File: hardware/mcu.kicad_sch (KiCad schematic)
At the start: 4 parts, among them U3 STM32G0C1KCTxN

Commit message: Fixes after review
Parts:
- added C1, C24: 100n, Capacitor_SMD:C_0603_1608Metric_Pad1.08x0.95mm_HandSolder, symbol Device:C_Small
- R10, R11, R9: value 1k -> 33R
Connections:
- net +3.3V: now also C1.1, C24.1
- net GND: now also C1.2, C24.2
- net VN_RX: now also U3.31 (PB7); no longer U3.30 (PB6)
- net VN_TX: now also U3.30 (PB6); no longer U3.31 (PB7)
- net VN_SNC_IN renamed VN_GNSS_SYNC
- net VN_SNC_OUT: no longer names the net of U3.2 (PC14)
- no-connect marks 7 -> 8

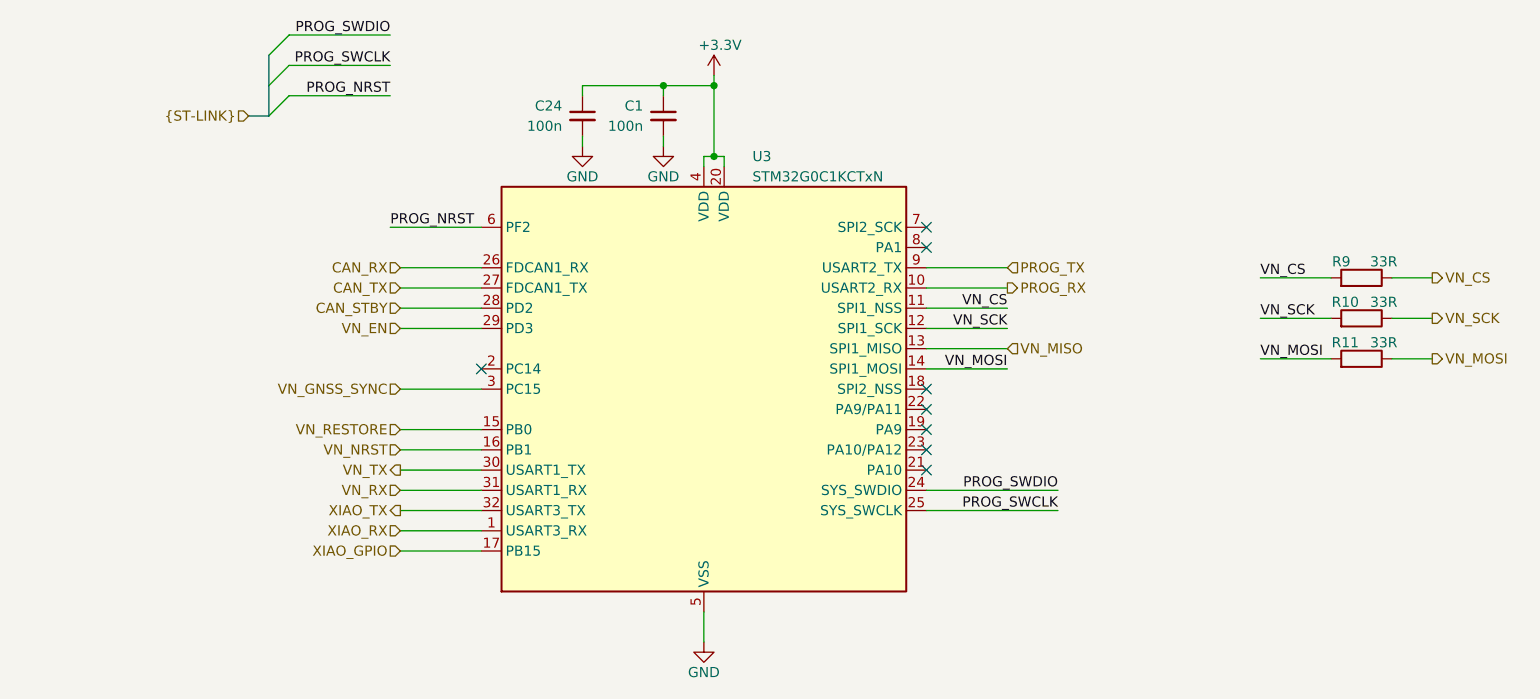
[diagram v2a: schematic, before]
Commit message: Fixes after review and mouser links for most components added
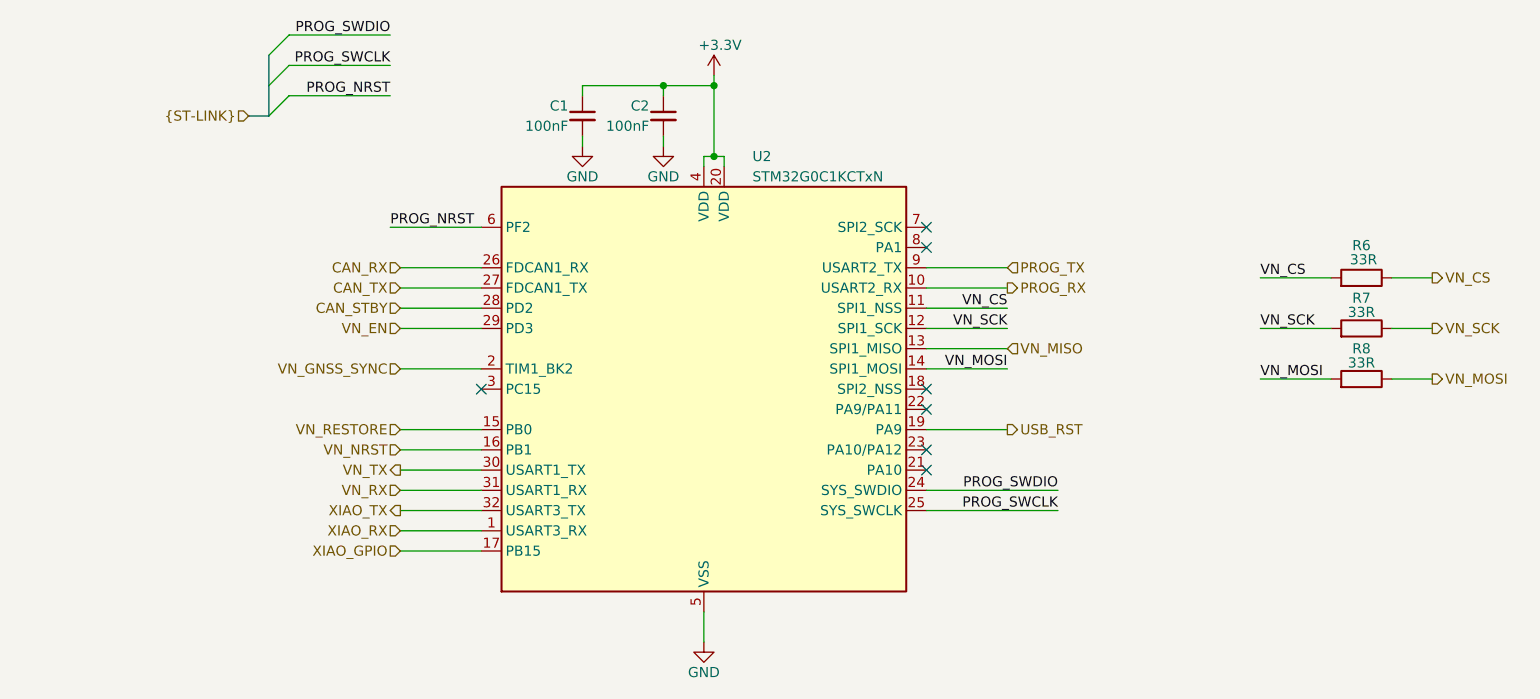
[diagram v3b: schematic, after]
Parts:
- C1: renamed from C24; value 100n -> 100nF
- C2: renamed from C1; value 100n -> 100nF
- R6: renamed from R9; footprint (none) -> Resistor_SMD:R_0603_1608Metric_Pad0.98x0.95mm_HandSolder; Mouser (none) -> https://www.mouser.pl/ProductDetail/YAGEO/RC0603FR-7W33RL?q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
- R7: renamed from R10; footprint (none) -> Resistor_SMD:R_0603_1608Metric_Pad0.98x0.95mm_HandSolder; Mouser (none) -> https://www.mouser.pl/ProductDetail/YAGEO/RC0603FR-7W33RL?q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
- R8: renamed from R11; footprint (none) -> Resistor_SMD:R_0603_1608Metric_Pad0.98x0.95mm_HandSolder; Mouser (none) -> https://www.mouser.pl/ProductDetail/YAGEO/RC0603FR-7W33RL?q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
- U2: renamed from U3; Mouser (none) -> https://www.mouser.pl/ProductDetail/STMicroelectronics/STM3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
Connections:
- net VN_GNSS_SYNC: now also U2.2 (PC14); no longer U2.3 (PC15)
- net USB_RST: now reaches U2.19 (PA9/UCPD1_DBCC1)
- no-connect marks 8 -> 7
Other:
- moved on the sheet: R7, R8

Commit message: changed some elements on shematic
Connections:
- net VN_GNSS_SYNC: now also U2.18 (PA8); no longer U2.2 (PC14)

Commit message: All components placed on pcb
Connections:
- net VN_CS: no longer R6.2, U2.11 (PA4)
- net VN_MOSI: no longer R8.2, U2.14 (PA7)
- net VN_SCK: no longer R7.2, U2.12 (PA5)
- new net vnCS: R6.2, U2.11 (PA4)
- new net vnMOSI: R8.2, U2.14 (PA7)
- new net vnSCK: R7.2, U2.12 (PA5)
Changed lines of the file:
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@@
 		)
 	)
-	(label "VN_SCK"
+	(label "vnSCK"
 		(at 171.45 90.17 180)
 		(effects
@@
 		)
 	)
-	(label "VN_CS"
+	(label "vnCS"
 		(at 203.2 83.82 0)
 		(effects
@@
 		)
 	)
-	(label "VN_MOSI"
+	(label "vnMOSI"
 		(at 203.2 96.52 0)
 		(effects
@@
 		)
 	)
-	(label "VN_CS"
+	(label "vnCS"
 		(at 171.45 87.63 180)
 		(effects
@@
 		)
 	)
-	(label "VN_SCK"
+	(label "vnSCK"
 		(at 203.2 90.17 0)
 		(effects
@@
 		)
 	)
-	(label "VN_MOSI"
+	(label "vnMOSI"
 		(at 171.45 95.25 180)
 		(effects

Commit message: Finished routing
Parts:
- added TP4: RSTR, TestPoint:TestPoint_Pad_D1.0mm, symbol Connector:TestPoint
- added TP5: NRST, TestPoint:TestPoint_Pad_D1.0mm, symbol Connector:TestPoint
- added TP6: EN, TestPoint:TestPoint_Pad_D1.0mm, symbol Connector:TestPoint
- added TP7: CS, TestPoint:TestPoint_Pad_D1.0mm, symbol Connector:TestPoint
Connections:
- net VN_EN: now also TP6.1
- net VN_NRST: now also TP5.1
- net VN_RESTORE: now also TP4.1
- net vnCS: now also TP7.1

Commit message: Some smaller fixes and final aesthetic changes
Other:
- company: Author: -> Author: Kacper Pawlak
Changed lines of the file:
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@@
 	(paper "A4")
 	(title_block
-		(company "Author:")
+		(company "Author: Kacper Pawlak")
+		(comment 1 "Reviewer: Piotr Lesicki")
 	)
 	(junction
